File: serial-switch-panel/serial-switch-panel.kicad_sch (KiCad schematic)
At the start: 59 parts, among them J10 Conn_01x01, J11 Conn_01x01, J12 Conn_01x01, J13 Conn_01x01, J14 Conn_01x01, J15 Conn_01x01, J16 Conn_01x01, J17 Conn_01x01, J18 Conn_01x01, J2 2501551-4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

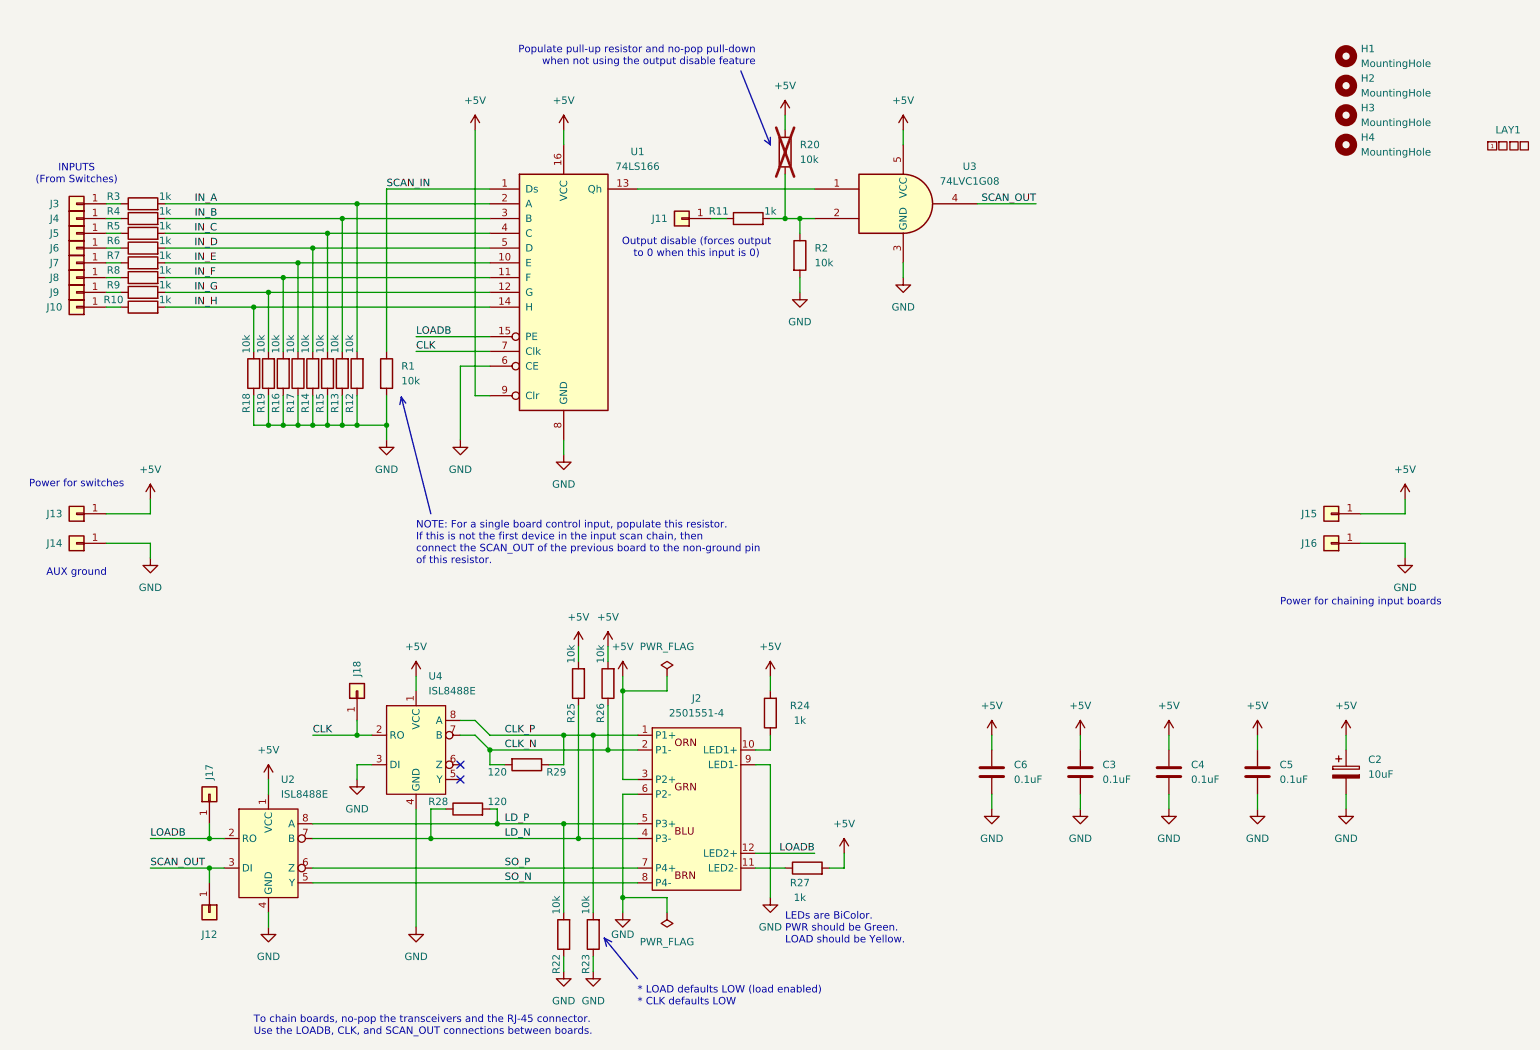
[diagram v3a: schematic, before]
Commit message: [fp] Complete board route
Note: lots of DRC errors & warnings.
- Warnings are silk overlaps - these are fine
- Most errors are clearance violations on the shift register - waving these as still > 6mil
- Remaining errors are thermal spokes on non-critical components & fill regions
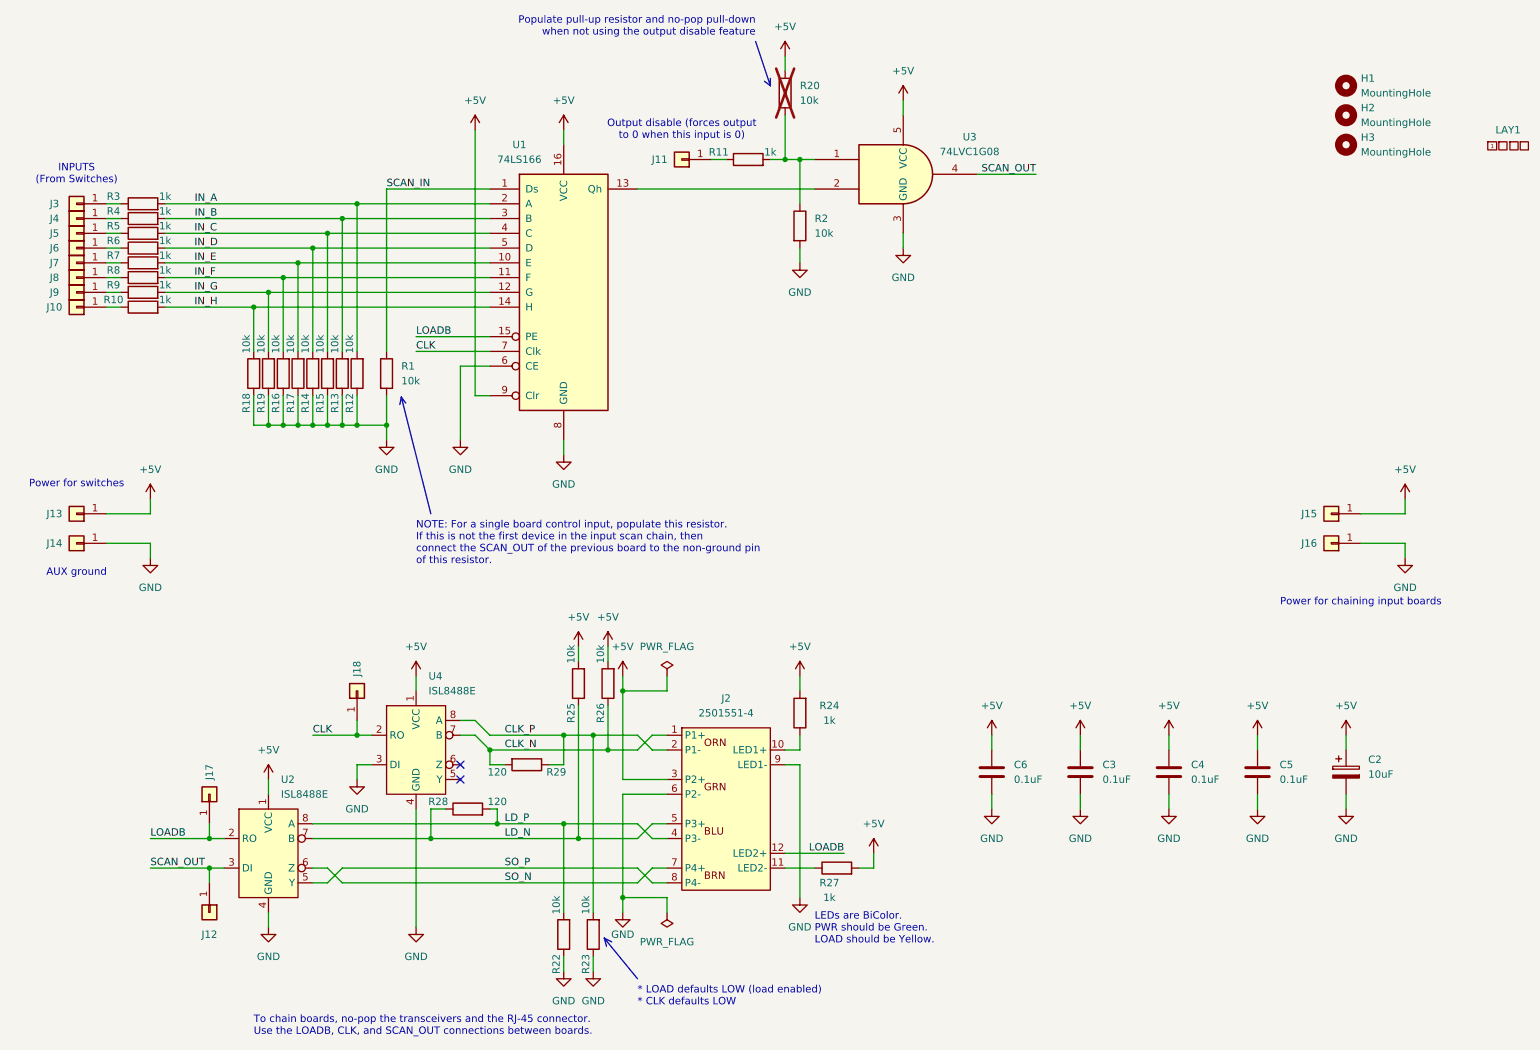
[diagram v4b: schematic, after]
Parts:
- removed H1: MountingHole, MountingHole:MountingHole_3.2mm_M3, symbol Mechanical:MountingHole
- C2: footprint Capacitor_THT:C_Radial_D8.0mm_H7.0mm_P3.50mm -> Capacitor_SMD:C_1206_3216Metric
- renumbered H2 to H1, H3 to H2, H4 to H3
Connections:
- net CLK_N: now also J2.1 (P1+); no longer J2.2 (P1-)
- net CLK_P: now also J2.2 (P1-); no longer J2.1 (P1+)
- net LD_N: now also J2.5 (P3+); no longer J2.4 (P3-)
- net LD_P: now also J2.4 (P3-); no longer J2.5 (P3+)
- net SO_N: now also J2.7 (P4+), U2.6 (Z); no longer J2.8 (P4-), U2.5 (Y)
- net SO_P: now also J2.8 (P4-), U2.5 (Y); no longer J2.7 (P4+), U2.6 (Z)
- net at R11.2, R2.1, R20.2: now also U3.1; no longer U3.2
- net at U1.13 (Qh): now also U3.2; no longer U3.1
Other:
- moved on the sheet: J11, J2, R11, R2, R20, R24, R27, U3

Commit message: [fp][rs] Change hole footprints to no soldermask
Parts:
- H1, H2, H3: footprint MountingHole:MountingHole_3.2mm_M3 -> CUSTOM:MountingHole_3.2mm_M3
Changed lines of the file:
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@@
 			)
 		)
-		(property "Footprint" "MountingHole:MountingHole_3.2mm_M3"
+		(property "Footprint" "CUSTOM:MountingHole_3.2mm_M3"
 			(at 243.84 38.1 0)
 			(hide yes)
@@
 			)
 		)
-		(property "Footprint" "MountingHole:MountingHole_3.2mm_M3"
+		(property "Footprint" "CUSTOM:MountingHole_3.2mm_M3"
 			(at 243.84 33.02 0)
 			(hide yes)
@@
 			)
 		)
-		(property "Footprint" "MountingHole:MountingHole_3.2mm_M3"
+		(property "Footprint" "CUSTOM:MountingHole_3.2mm_M3"
 			(at 243.84 27.94 0)
 			(hide yes)

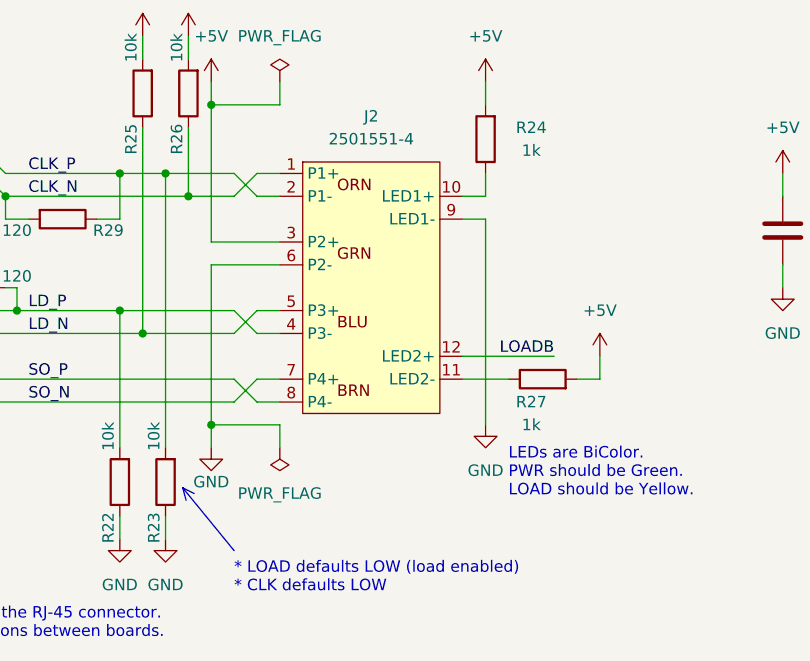
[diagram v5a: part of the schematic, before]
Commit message: [fp] Add RJ-45 shield connection
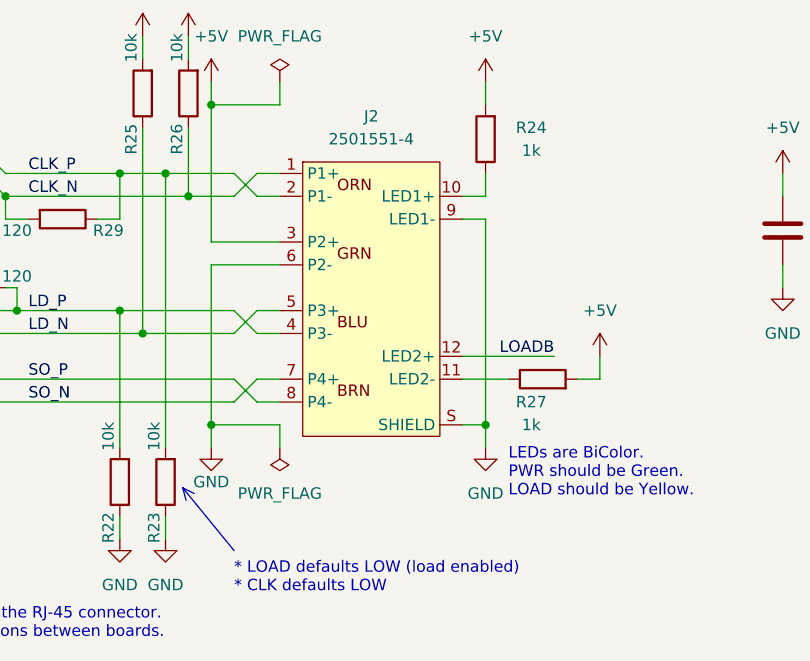
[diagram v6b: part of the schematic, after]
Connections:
- net GND: now also J2.S (SHIELD)
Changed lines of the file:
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@@
 	)
 	(junction
+		(at 149.86 167.64)
+		(diameter 0)
+		(color 0 0 0 0)
+	)
+	(junction
 		(at 86.36 157.48)
 		(diameter 0)
@@
 	(wire
 		(pts
+			(xy 149.86 167.64) (xy 149.86 170.18)
+		)
+		(stroke
+			(width 0)
+			(type default)
+		)
+	)
+	(wire
+		(pts
 			(xy 73.66 48.26) (xy 73.66 73.66)
 		)
@@
 	(wire
 		(pts
+			(xy 147.32 167.64) (xy 149.86 167.64)
+		)
+		(stroke
+			(width 0)
+			(type default)
+		)
+	)
+	(wire
+		(pts
 			(xy 147.32 142.24) (xy 149.86 142.24)
 		)
@@
 		)
 		(instances
-			(project ""
+			(project "serial-switch-panel"
 				(path "/6e8e0d39-e51b-4511-a712-1d92a774977f"
 					(reference "LAY1")
@@
 		)
 		(instances
-			(project ""
+			(project "serial-switch-panel"
 				(path "/6e8e0d39-e51b-4511-a712-1d92a774977f"
 					(reference "#PWR01")
@@
 	(symbol
 		(lib_id "power:GND")
-		(at 149.86 167.64 0)
+		(at 149.86 170.18 0)
 		(unit 1)
 		(body_style 1)
@@
 		(fields_autoplaced yes)
 		(property "Reference" "#PWR025"
-			(at 149.86 173.99 0)
+			(at 149.86 176.53 0)
 			(hide yes)
 			(show_name no)
@@
 		)
 		(property "Value" "GND"
-			(at 149.86 172.72 0)
+			(at 149.86 175.26 0)
 			(show_name no)
 			(do_not_autoplace no)
@@
 		)
 		(property "Footprint" ""
-			(at 149.86 167.64 0)
+			(at 149.86 170.18 0)
 			(hide yes)
 			(show_name no)
@@
 		)
 		(property "Datasheet" ""
-			(at 149.86 167.64 0)
+			(at 149.86 170.18 0)
 			(hide yes)
 			(show_name no)
@@
 		)
 		(property "Description" "Power symbol creates a global label with name \"GND\" , ground"
-			(at 149.86 167.64 0)
+			(at 149.86 170.18 0)
 			(hide yes)
 			(show_name no)
@@
 		(pin "3"
 		)
+		(pin "S"
+		)
 		(instances
-			(project ""
+			(project "serial-switch-panel"
 				(path "/6e8e0d39-e51b-4511-a712-1d92a774977f"
 					(reference "J2")
@@
 		)
 		(instances
-			(project ""
+			(project "serial-switch-panel"
 				(path "/6e8e0d39-e51b-4511-a712-1d92a774977f"
 					(reference "U1")
@@
 		)
 		(instances
-			(project ""
+			(project "serial-switch-panel"
 				(path "/6e8e0d39-e51b-4511-a712-1d92a774977f"
 					(reference "U3")
@@
 		)
 		(instances
-			(project ""
+			(project "serial-switch-panel"
 				(path "/6e8e0d39-e51b-4511-a712-1d92a774977f"
 					(reference "R1")
@@
 		)
 		(instances
-			(project ""
+			(project "serial-switch-panel"
 				(path "/6e8e0d39-e51b-4511-a712-1d92a774977f"
 					(reference "C3")
@@
 		)
 		(instances
-			(project ""
+			(project "serial-switch-panel"
 				(path "/6e8e0d39-e51b-4511-a712-1d92a774977f"
 					(reference "#FLG01")
@@
 		)
 		(instances
-			(project ""
+			(project "serial-switch-panel"
 				(path "/6e8e0d39-e51b-4511-a712-1d92a774977f"
 					(reference "#PWR02")
@@
 		)
 		(instances
-			(project ""
+			(project "serial-switch-panel"
 				(path "/6e8e0d39-e51b-4511-a712-1d92a774977f"
 					(reference "U2")

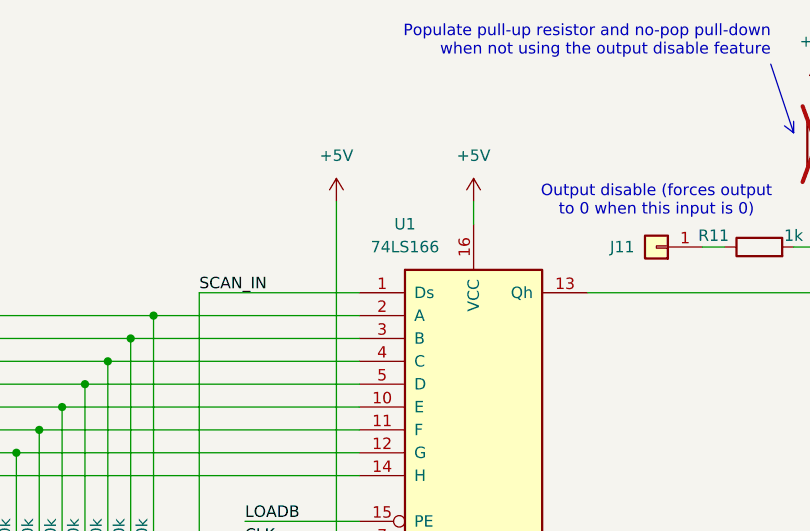
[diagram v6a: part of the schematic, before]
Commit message: [fp] Change '166 to SOIC-16 footprint; Export v1.0A1 gerbers
Wow, that one is tight (!)
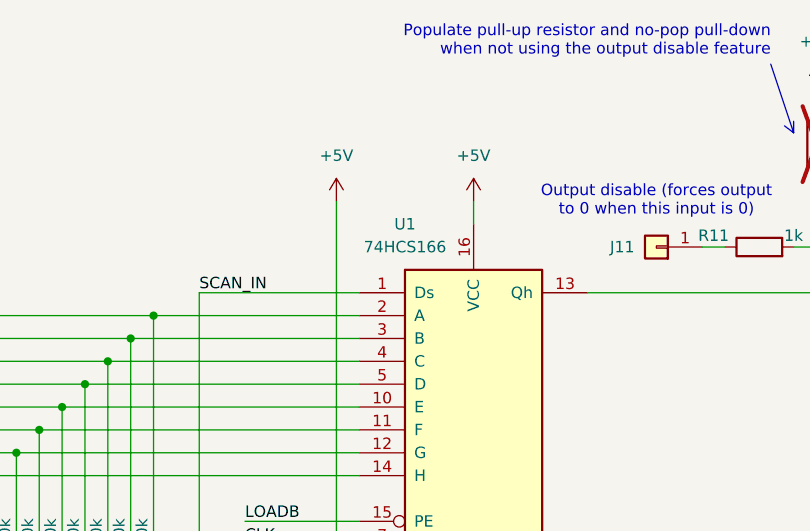
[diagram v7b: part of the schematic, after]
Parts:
- U1: value 74LS166 -> 74HCS166; footprint Package_SO:Texas_DYY0016A_TSOT-23-16_2x4.2mm_P0.5mm -> Package_SO:SOIC-16_3.9x9.9mm_P1.27mm
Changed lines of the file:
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@@
 			)
 		)
-		(property "Value" "74LS166"
+		(property "Value" "74HCS166"
 			(at 101.6 40.64 0)
 			(show_name no)
@@
 			)
 		)
-		(property "Footprint" "Package_SO:Texas_DYY0016A_TSOT-23-16_2x4.2mm_P0.5mm"
+		(property "Footprint" "Package_SO:SOIC-16_3.9x9.9mm_P1.27mm"
 			(at 109.22 63.5 0)
 			(hide yes)
